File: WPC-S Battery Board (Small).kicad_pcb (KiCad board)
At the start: 2 copper layers, 54 x 44.9 mm, 6 parts, among them J101 Conn_01x05

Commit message: Specify JLC order number location
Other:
- board text added: "JLCJLCJLCJLC"
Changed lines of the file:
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@@
   (gr_line (start 142.6 85.22) (end 94.1 85.22)
     (stroke (width 0.1) (type default)) (layer "Edge.Cuts"))
+  (gr_text "JLCJLCJLCJLC" (at 123.617858 71.57175) (layer "B.SilkS")
+    (effects (font (size 1 1) (thickness 0.15)) (justify left bottom mirror))
+  )
   (gr_text "bdash's battery board\nWPC-S ${VERSION}" (at 118.35 55.26) (layer "F.SilkS")
     (effects (font (face "Menlo") (size 1.25 1.25) (thickness 0.25) bold) (justify bottom))

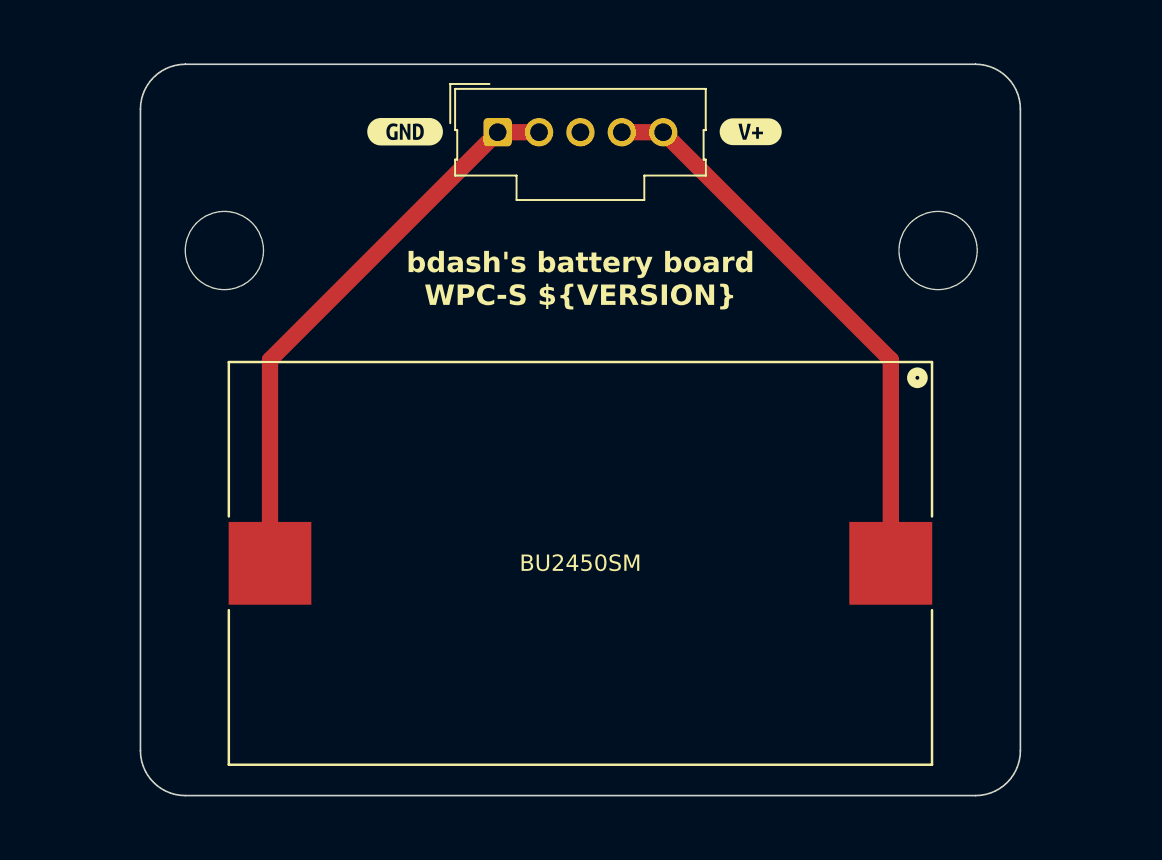
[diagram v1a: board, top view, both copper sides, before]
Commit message: Copper fills to make the board look nicer.
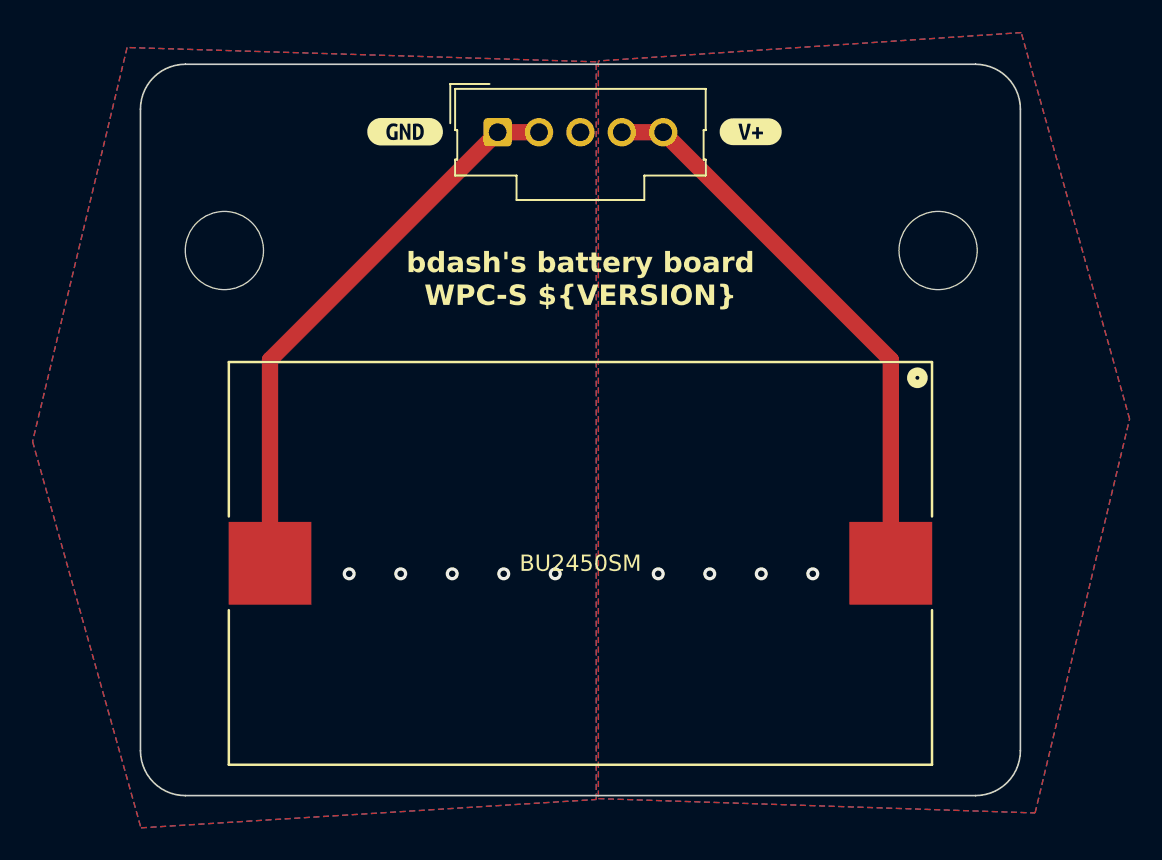
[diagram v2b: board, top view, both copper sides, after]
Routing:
- net /V+: vias 0 -> 4
- net /GND: vias 0 -> 5
- added copper zone on B.Cu, net /GND
- added copper zone on F.Cu, net /GND
- added copper zone on B.Cu, net /V+
- added copper zone on F.Cu, net /V+
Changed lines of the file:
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@@
   (segment (start 123.43 44.51) (end 120.89 44.51) (width 1) (layer "F.Cu") (net 2))
   (segment (start 137.4 72.84) (end 137.4 58.48) (width 1) (layer "F.Cu") (net 2))
+  (via (at 132.61 71.61) (size 0.8) (drill 0.4) (layers "F.Cu" "B.Cu") (free) (net 2))
+  (via (at 123.126666 71.61) (size 0.8) (drill 0.4) (layers "F.Cu" "B.Cu") (free) (net 2))
+  (via (at 126.287777 71.61) (size 0.8) (drill 0.4) (layers "F.Cu" "B.Cu") (free) (net 2))
+  (via (at 129.448888 71.61) (size 0.8) (drill 0.4) (layers "F.Cu" "B.Cu") (free) (net 2))
   (segment (start 99.3 58.48) (end 113.27 44.51) (width 1) (layer "F.Cu") (net 3))
   (segment (start 113.27 44.51) (end 115.81 44.51) (width 1) (layer "F.Cu") (net 3))
   (segment (start 99.3 72.84) (end 99.3 58.48) (width 1) (layer "F.Cu") (net 3))
+  (via (at 116.804444 71.61) (size 0.8) (drill 0.4) (layers "F.Cu" "B.Cu") (free) (net 3))
+  (via (at 110.482222 71.61) (size 0.8) (drill 0.4) (layers "F.Cu" "B.Cu") (free) (net 3))
+  (via (at 107.321111 71.61) (size 0.8) (drill 0.4) (layers "F.Cu" "B.Cu") (free) (net 3))
+  (via (at 104.16 71.61) (size 0.8) (drill 0.4) (layers "F.Cu" "B.Cu") (free) (net 3))
+  (via (at 113.643333 71.61) (size 0.8) (drill 0.4) (layers "F.Cu" "B.Cu") (free) (net 3))
+  (zone (net 2) (net_name "/V+") (layers "F&B.Cu") (hatch edge 0.5)
+    (connect_pads (clearance 0.5))
+    (min_thickness 0.25) (filled_areas_thickness no)
+    (fill yes (thermal_gap 0.5) (thermal_bridge_width 0.5))
+    (polygon
+      (pts
+        (xy 119.452488 85.405646)
+        (xy 146.252488 86.285646)
+        (xy 152.052488 62.105646)
+        (xy 145.402488 38.395646)
+        (xy 119.452488 40.135646)
+      )
+    )
+  )
+  (zone (net 3) (net_name "/GND") (layers "F&B.Cu") (hatch edge 0.5)
+    (connect_pads (clearance 0.5))
+    (min_thickness 0.25) (filled_areas_thickness no)
+    (fill yes (thermal_gap 0.5) (thermal_bridge_width 0.5))
+    (polygon
+      (pts
+        (xy 119.32 40.19)
+        (xy 90.53 39.31)
+        (xy 84.73 63.49)
+        (xy 91.38 87.2)
+        (xy 119.32 85.46)
+      )
+    )
+  )
 )
